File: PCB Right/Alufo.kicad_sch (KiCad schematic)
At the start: 32 parts, among them J2 USB_C_Receptacle_USB2.0_16P_2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, J4 USB_C_Receptacle_USB2.0_16P_2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, SW2 BOOT, U2 CH552T, U4 USBLC6-2P6, U6 USBLC6-2P6

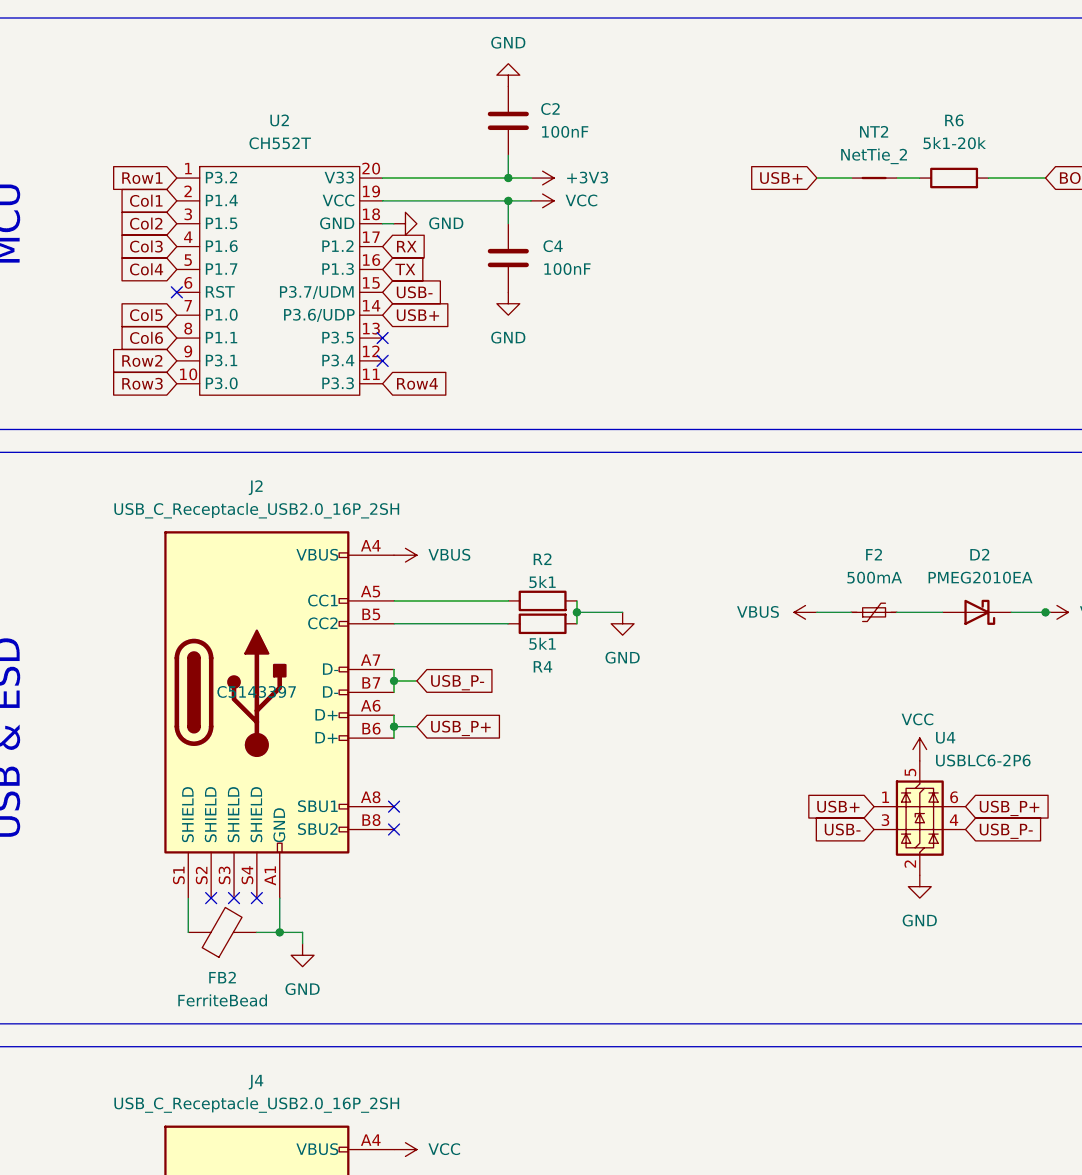
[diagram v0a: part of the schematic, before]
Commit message: Move righthand USB port in
Moved port and associated components 19.05÷12mm left to account for SMD legs.
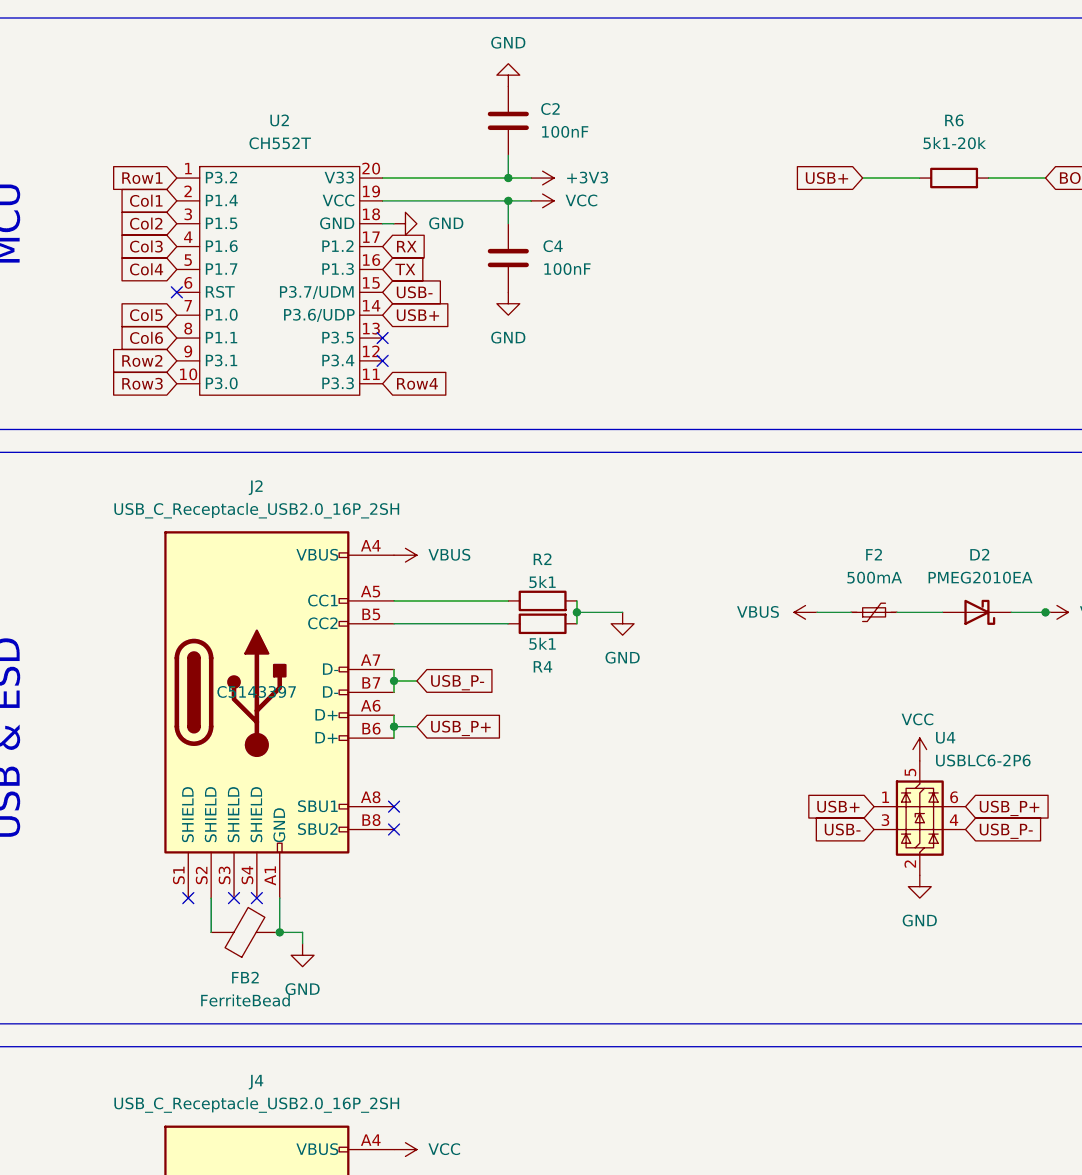
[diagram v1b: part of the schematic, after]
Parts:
- removed NT2: NetTie_2, Project_Library:NetTie-2_SMD_Pad0.2mm, symbol Device:NetTie_2
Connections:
- net USB+: now also R6.1
- net at J2.S1 (SHIELD): no longer FB2.1
- net at J2.S2 (SHIELD): now also FB2.1
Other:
- moved on the sheet: FB2
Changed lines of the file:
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@@
 	)
 	(junction
-		(at 49.53 127)
+		(at 62.23 170.18)
 		(diameter 0)
 		(color 0 0 0 0)
 	)
 	(junction
-		(at 62.23 170.18)
+		(at 134.62 91.44)
 		(diameter 0)
 		(color 0 0 0 0)
 	)
 	(junction
-		(at 134.62 91.44)
+		(at 49.53 127)
 		(diameter 0)
 		(color 0 0 0 0)
@@
 	)
 	(no_connect
-		(at 46.99 123.19)
-	)
-	(no_connect
 		(at 62.23 181.61)
 	)
@@
 	)
 	(no_connect
-		(at 62.23 156.21)
+		(at 46.99 123.19)
 	)
 	(no_connect
-		(at 41.91 123.19)
+		(at 62.23 156.21)
 	)
 	(no_connect
@@
 	)
 	(no_connect
+		(at 39.37 123.19)
+	)
+	(no_connect
 		(at 44.45 123.19)
 	)
@@
 	(wire
 		(pts
-			(xy 39.37 127) (xy 39.37 123.19)
+			(xy 41.91 123.19) (xy 41.91 127)
 		)
 		(stroke
@@
 	(wire
 		(pts
-			(xy 49.53 127) (xy 46.99 127)
-		)
-		(stroke
-			(width 0)
-			(type default)
-		)
-	)
-	(wire
-		(pts
-			(xy 109.22 43.18) (xy 113.03 43.18)
+			(xy 114.3 43.18) (xy 120.65 43.18)
 		)
 		(stroke
@@
 	(wire
 		(pts
-			(xy 118.11 43.18) (xy 120.65 43.18)
-		)
-		(stroke
-			(width 0)
-			(type default)
-		)
-	)
-	(wire
-		(pts
 			(xy 62.23 104.14) (xy 62.23 105.41)
 		)
@@
 	(global_label "USB+"
 		(shape input)
-		(at 109.22 43.18 180)
+		(at 114.3 43.18 180)
 		(fields_autoplaced yes)
 		(effects
@@
 		)
 		(property "Intersheetrefs" "${INTERSHEET_REFS}"
-			(at 100.8524 43.18 0)
+			(at 105.9324 43.18 0)
 			(effects
 				(font
@@
 	(symbol
 		(lib_id "Device:FerriteBead")
-		(at 43.18 127 90)
+		(at 45.72 127 90)
 		(unit 1)
 		(exclude_from_sim no)
@@
 		(dnp no)
 		(property "Reference" "FB2"
-			(at 43.18 132.08 90)
+			(at 45.72 132.08 90)
 			(effects
 				(font
@@
 		)
 		(property "Value" "FerriteBead"
-			(at 43.18 134.62 90)
+			(at 45.72 134.62 90)
 			(effects
 				(font
@@
 		)
 		(property "Footprint" "Inductor_SMD:L_0805_2012Metric"
-			(at 43.18 128.778 90)
+			(at 45.72 128.778 90)
 			(effects
 				(font
@@
 		)
 		(property "Datasheet" "~"
-			(at 43.18 127 0)
+			(at 45.72 127 0)
 			(effects
 				(font
@@
 		)
 		(property "Description" "Ferrite bead"
-			(at 43.18 127 0)
+			(at 45.72 127 0)
 			(effects
 				(font
@@
 		)
 		(property "LCSC" "C20416196"
-			(at 43.18 127 0)
+			(at 45.72 127 0)
 			(effects
 				(font
@@
 					(unit 1)
 				)
-			)
-		)
-	)
-	(symbol
-		(lib_id "Device:NetTie_2")
-		(at 115.57 43.18 0)
-		(unit 1)
-		(exclude_from_sim no)
-		(in_bom no)
-		(on_board yes)
-		(dnp no)
-		(property "Reference" "NT2"
-			(at 115.57 38.1 0)
-			(effects
-				(font
-					(size 1.27 1.27)
-				)
-			)
-		)
-		(property "Value" "NetTie_2"
-			(at 115.57 40.64 0)
-			(effects
-				(font
-					(size 1.27 1.27)
-				)
-			)
-		)
-		(property "Footprint" "Project_Library:NetTie-2_SMD_Pad0.2mm"
-			(at 115.57 43.18 0)
-			(effects
-				(font
-					(size 1.27 1.27)
-				)
-				(hide yes)
-			)
-		)
-		(property "Datasheet" "~"
-			(at 115.57 43.18 0)
-			(effects
-				(font
-					(size 1.27 1.27)
-				)
-				(hide yes)
-			)
-		)
-		(property "Description" "Net tie, 2 pins"
-			(at 115.57 43.18 0)
-			(effects
-				(font
-					(size 1.27 1.27)
-				)
-				(hide yes)
-			)
-		)
-		(pin "2"
-		)
-		(pin "1"
-		)
-		(instances
-			(project "Alufo"
-				(path "/52f043ac-ccff-4c85-bc10-2db9d3c9e3f3"
-					(reference "NT2")
-					(unit 1)
-				)

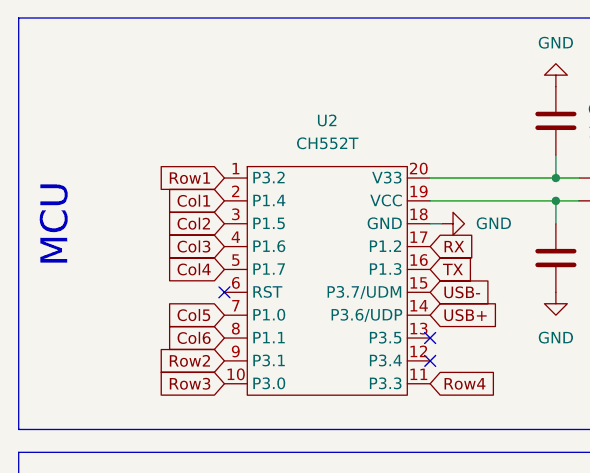
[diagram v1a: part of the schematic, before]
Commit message: Remove righthand R11
Col1 now routed under MCU between K11 and K21 instead of through jumper.
Row1 and Col1 pins on MCU swapped.
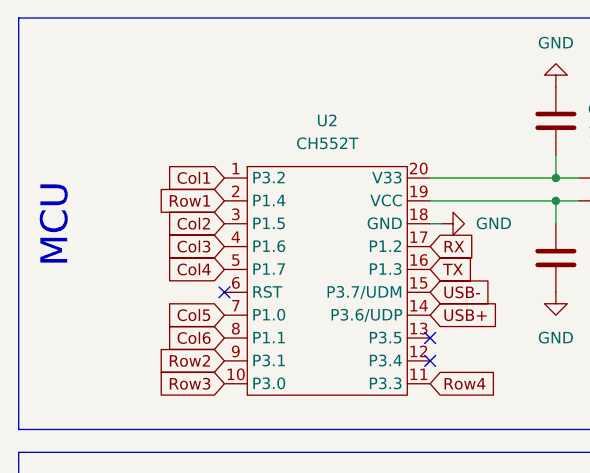
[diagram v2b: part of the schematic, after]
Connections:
- net Col1: now also U2.1 (P3.2); no longer U2.2 (P1.4)
- net Row1: now also U2.2 (P1.4); no longer U2.1 (P3.2)
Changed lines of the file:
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@@
 	(global_label "Row1"
 		(shape input)
-		(at 38.1 43.18 180)
+		(at 38.1 45.72 180)
 		(fields_autoplaced yes)
 		(effects
@@
 		)
 		(property "Intersheetrefs" "${INTERSHEET_REFS}"
-			(at 30.1558 43.18 0)
+			(at 30.1558 45.72 0)
 			(effects
 				(font
@@
 	(global_label "Col1"
 		(shape input)
-		(at 38.1 45.72 180)
+		(at 38.1 43.18 180)
 		(fields_autoplaced yes)
 		(effects
@@
 		)
 		(property "Intersheetrefs" "${INTERSHEET_REFS}"
-			(at 30.8211 45.72 0)
+			(at 30.8211 43.18 0)
 			(effects
 				(font

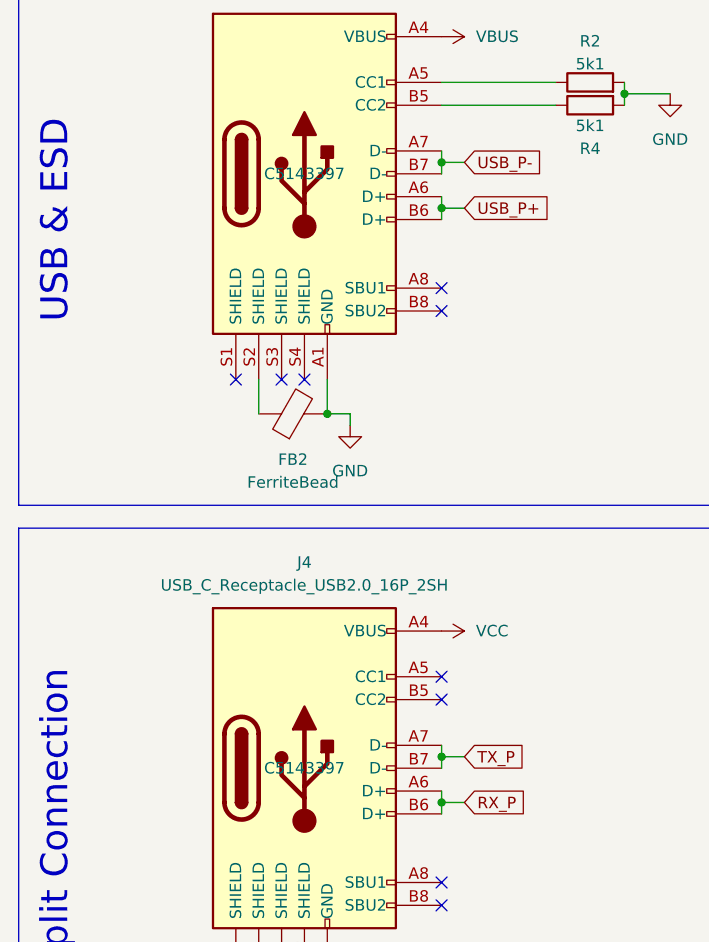
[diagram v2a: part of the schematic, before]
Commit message: Update LCSC part number for USB ports
Also hide LCSC numbers erroneously showing in schematic.
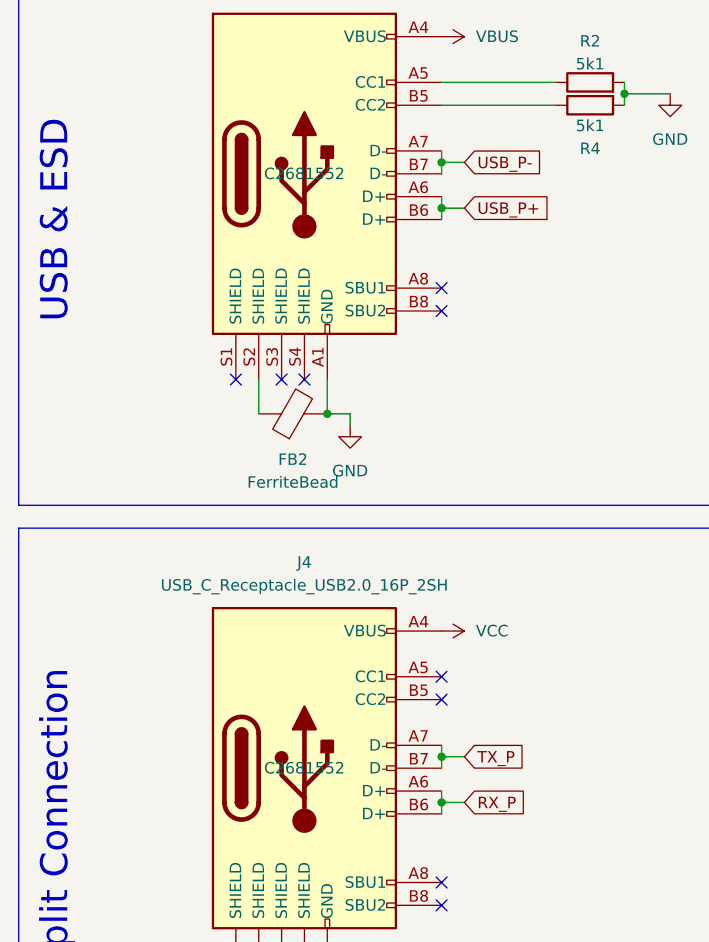
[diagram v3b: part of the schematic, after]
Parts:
- J2, J4: LCSC C5143397 -> C2681552
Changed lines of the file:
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@@
 			)
 		)
-		(property "LCSC" "C5143397"
+		(property "LCSC" "C2681552"
 			(at 46.99 100.33 0)
 			(effects
@@
 			)
 		)
-		(property "LCSC" "C5143397"
+		(property "LCSC" "C2681552"
 			(at 46.99 166.37 0)
 			(effects
